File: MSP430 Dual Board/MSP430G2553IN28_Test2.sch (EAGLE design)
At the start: 65 parts, among them IC1 MSP430, IC2 FM25640BSO8, IC3 7805TV, IC4 MSP430, IC5 DAC6311, IC6 CUSTOM_REGULATOR

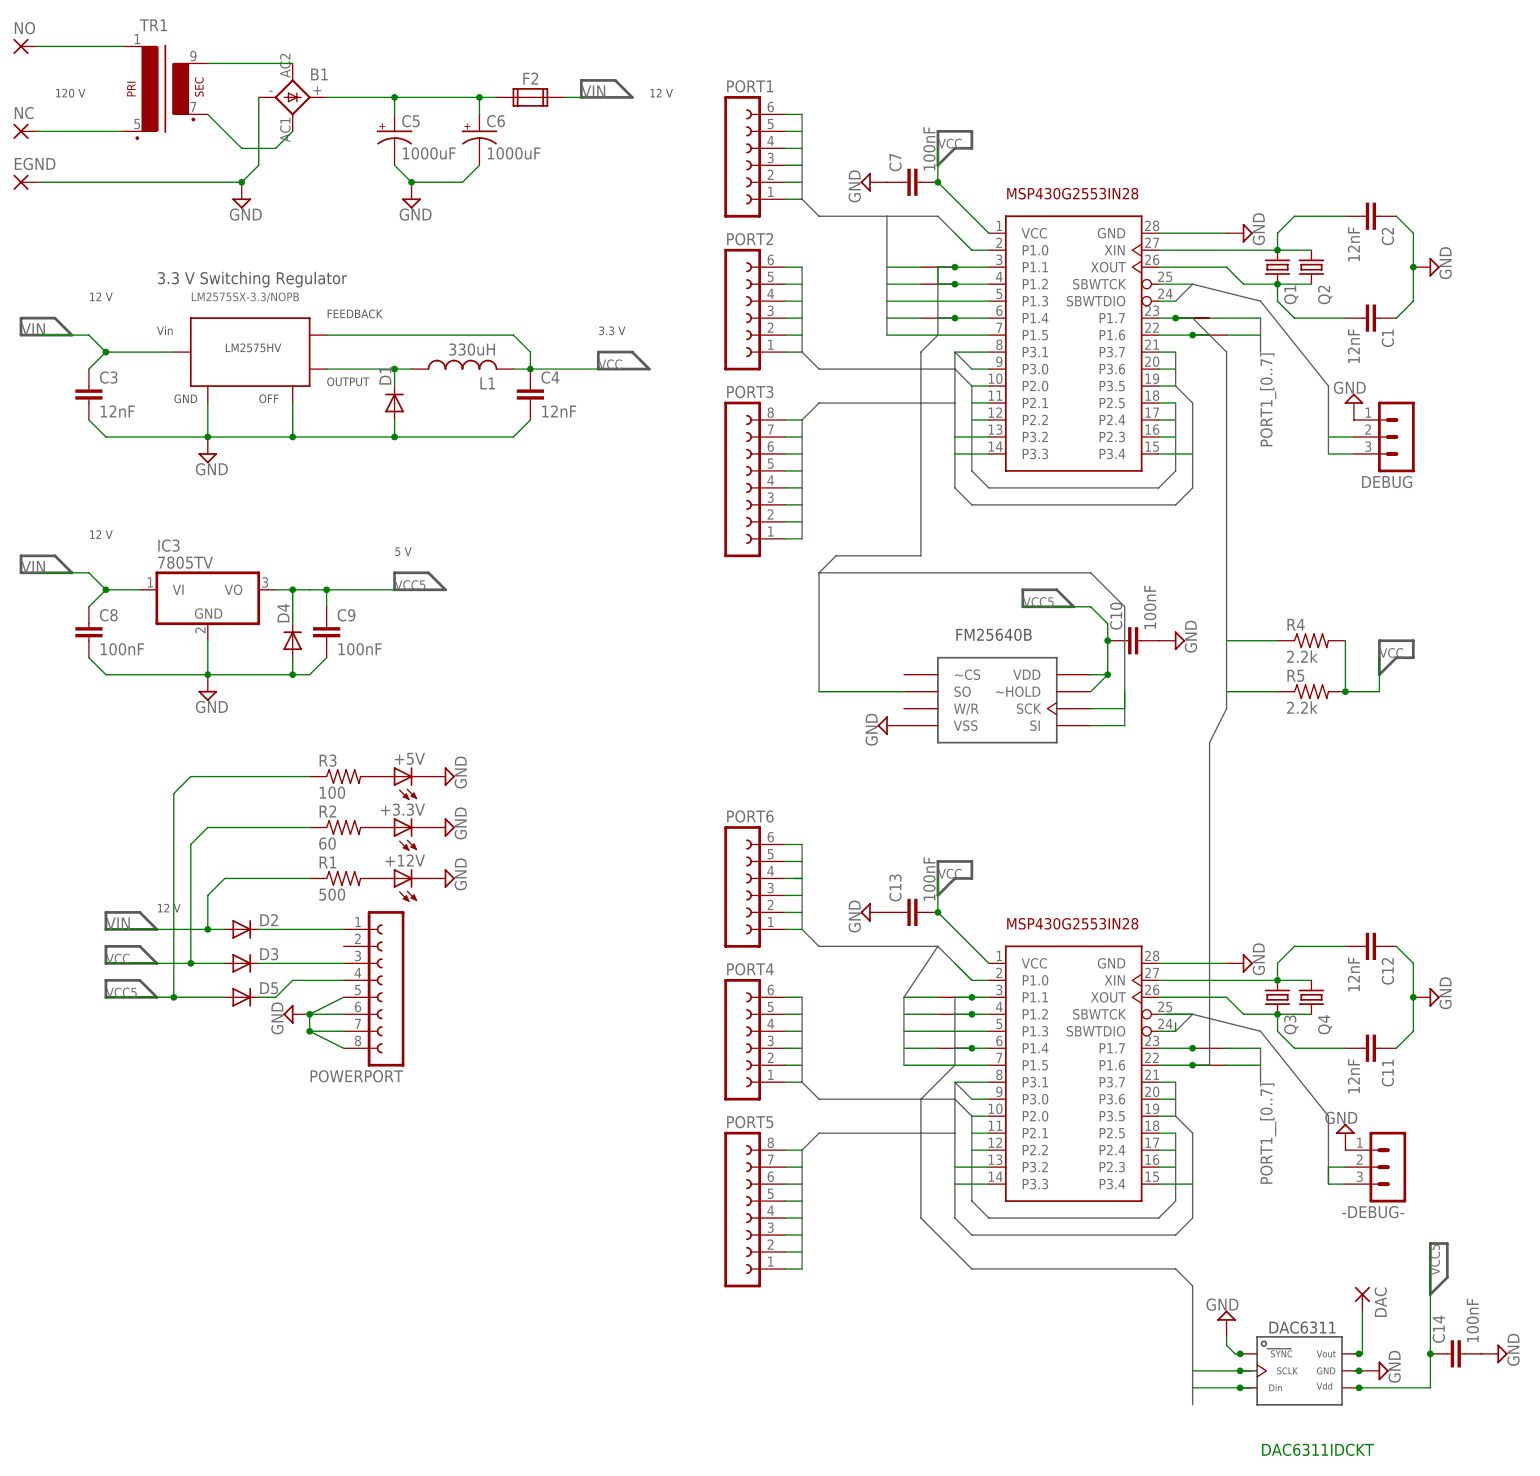
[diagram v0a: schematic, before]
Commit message: Fully Routed MSP430 Dual Board
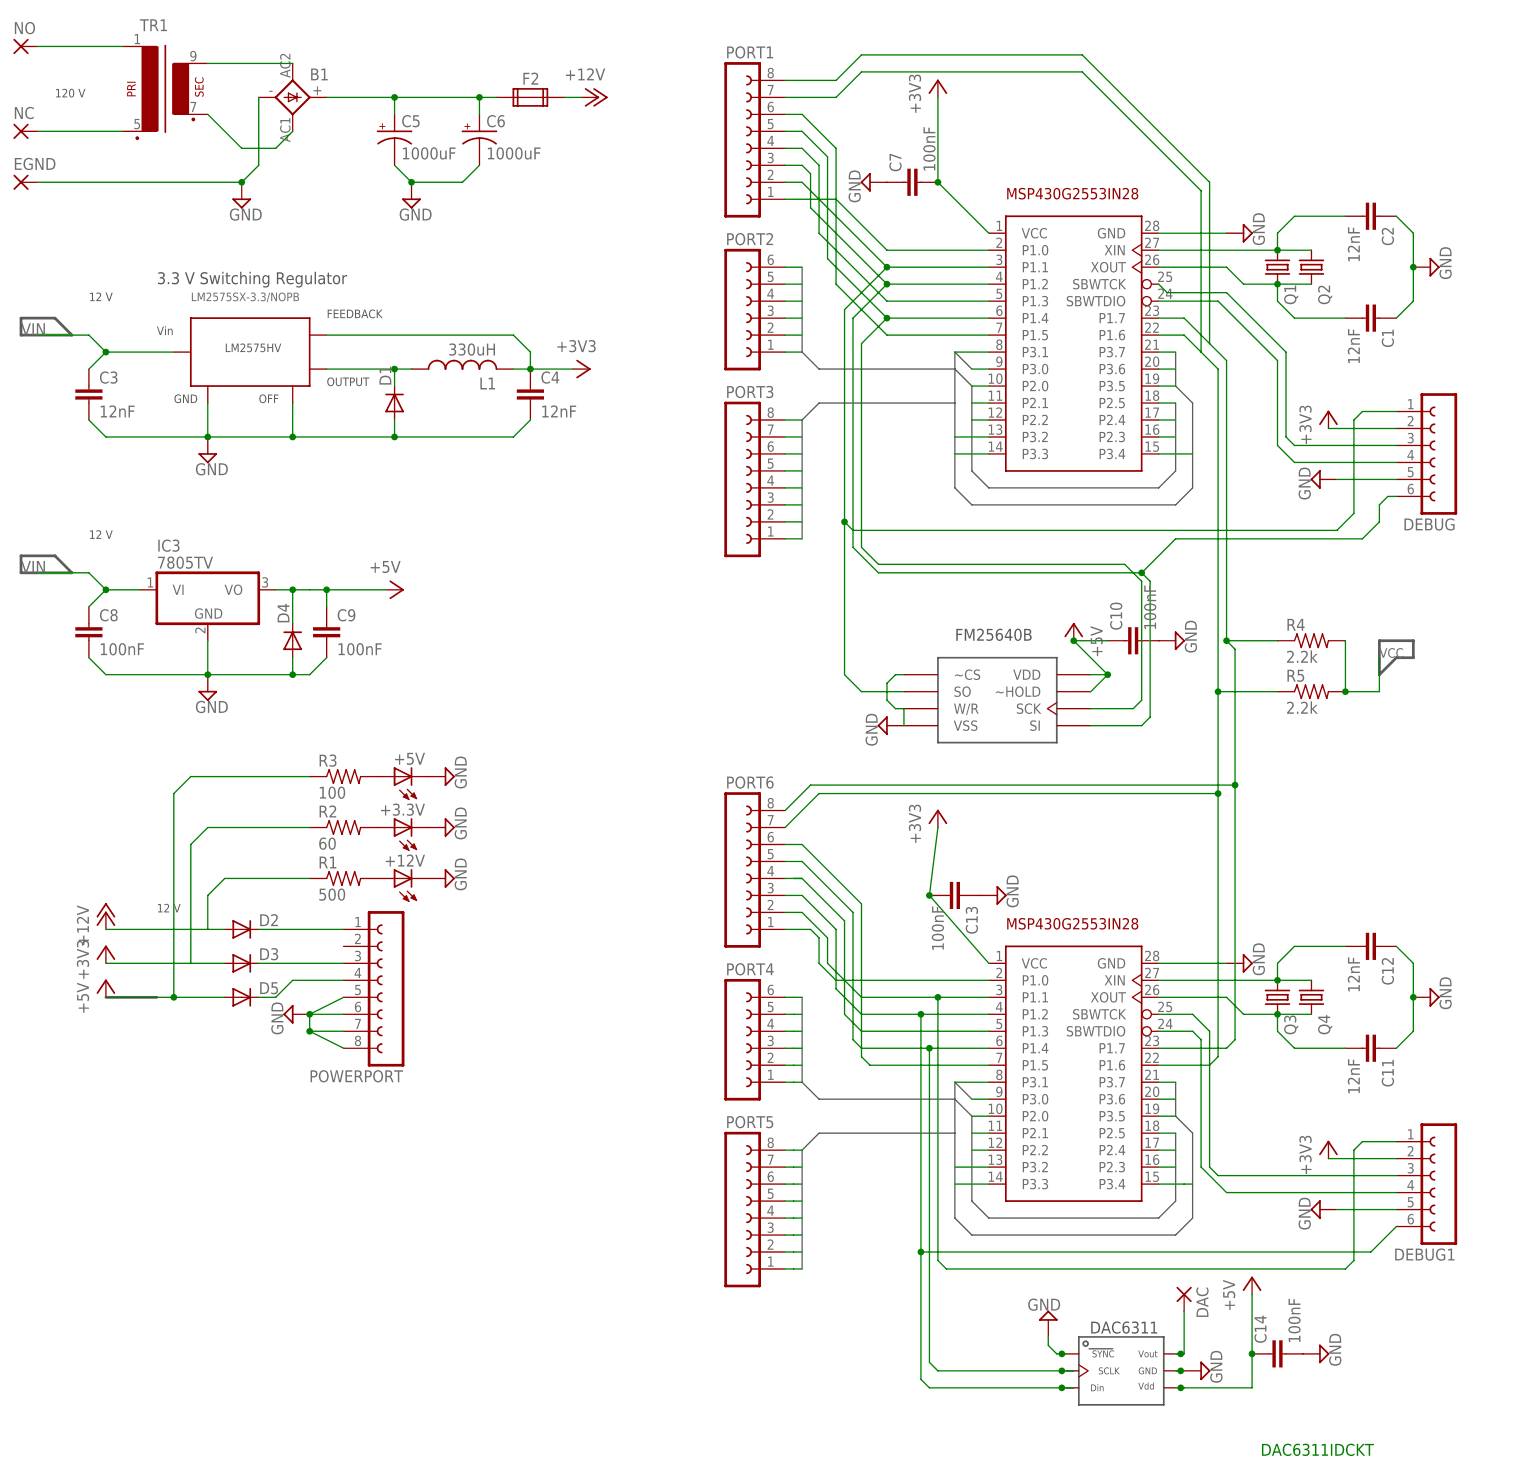
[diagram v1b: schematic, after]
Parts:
- removed -DEBUG-: (no value), con-lstb:MA03-1
- removed U$1, U$10, U$11, U$12, U$13, U$14, U$15, U$6, U$7, U$8, U$9: SHORTSHORT, msp430_board:SHORTSHORT
- added DEBUG1: (no value), con-lsta:FE06-1
- DEBUG: device con-lstb:MA03-1 -> con-lsta:FE06-1
- PORT1, PORT6: device con-lsta:FE06-1 -> con-lsta:FE08-1
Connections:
- removed net DEBUG_P1: DEBUG.2, IC1.SBWTCK
- removed net DEBUG_P2: DEBUG.3, IC1.SBWTDIO
- removed net DEBUG_P4: -DEBUG-.3, IC4.SBWTDIO
- removed net DEBUG_P_2: -DEBUG-.2, IC4.SBWTCK
- removed net PORT1_6: U$10.P$2
- removed net PORT1_7: U$8.P$2, U$9.P$2
- removed net PORT1__6: U$15.P$2
- removed net PORT1__7: U$14.P$2
- removed net PORT2_6: PORT4.1
- removed net SPI3: IC1.P1.1, IC2.SO, IC4.P1.1, IC5.P$3, U$1.P$2, U$11.P$2
- removed net SPI4: IC1.P1.2, IC2.SI, IC4.P1.2, U$12.P$2, U$6.P$2
- removed net SPI5: IC1.P1.4, IC2.SCK, IC4.P1.4, IC5.P$2, U$13.P$2, U$7.P$2
- new net +12V: D2.A, F2.2A, R1.1
- new net +3V3: C13.2, C4.1, C7.2, D3.A, DEBUG1.2, IC1.VCC, IC4.VCC, IC6.P$4, L1.2, R2.1
- new net +5V: C10.1, C14.1, C9.1, D5.A, IC2.VDD, IC2.~HOLD, IC5.P$4, R3.1
- new net N$20: DEBUG1.3, IC4.SBWTCK
- new net N$21: DEBUG1.4, IC4.SBWTDIO
- new net N$22: DEBUG.3, IC1.SBWTCK
- new net N$23: DEBUG.4, IC1.SBWTDIO
- net GND: now also DEBUG.5, DEBUG1.5, IC2.W/R, IC2.~CS; no longer -DEBUG-.1, DEBUG.1
- net I2C0: now also PORT1.8, PORT6.8; no longer U$14.P$1, U$8.P$1, U$9.P$1
- net I2C1: now also PORT1.7, PORT6.7; no longer U$10.P$1, U$15.P$1
- net PORT1_1: now also DEBUG.1, IC1.P1.1, IC2.SO; no longer U$1.P$1
- net PORT1_2: now also DEBUG.6, IC1.P1.2, IC2.SI; no longer U$6.P$1
- net PORT1_4: now also IC1.P1.4, IC2.SCK; no longer U$7.P$1
- net PORT1__1: now also DEBUG1.1, IC4.P1.1; no longer U$11.P$1
- net PORT1__2: now also DEBUG1.6, IC4.P1.2, IC5.P$3; no longer U$12.P$1
- net PORT1__4: now also IC4.P1.4, IC5.P$2; no longer U$13.P$1
- net PORT2__0: now also PORT4.1
- net VCC: no longer C13.2, C4.1, C7.2, D3.A, IC1.VCC, IC4.VCC, IC6.P$4, L1.2, R2.1
- net VCC5: no longer C10.1, C14.1, C9.1, D5.A, IC2.VDD, IC2.~HOLD, IC5.P$4, R3.1
- net VIN: no longer D2.A, F2.2A, R1.1
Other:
- note removed: "3.3 V"
- note removed: "5 V"
- moved on the sheet: C13, C14, DAC
